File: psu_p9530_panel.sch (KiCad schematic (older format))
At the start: 58 parts, among them IC306 LTC1658, IC308 CD4052B, IC310 TLC272, IC312 TLC272, U401 54LS164

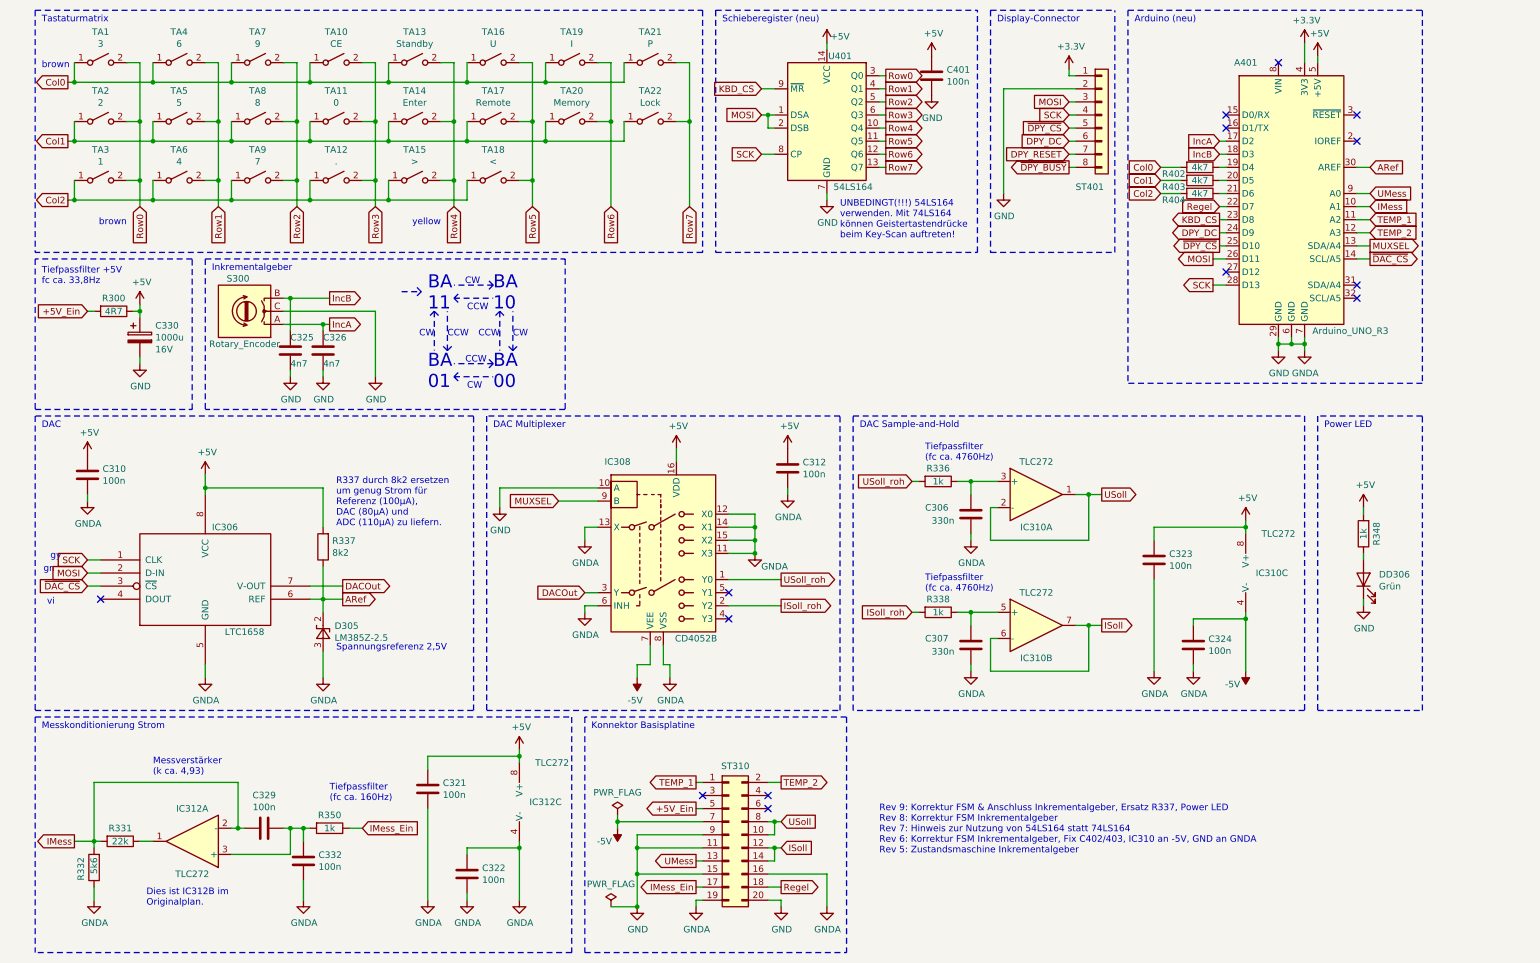
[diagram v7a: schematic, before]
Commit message: Schematic update: Display Shield Connections
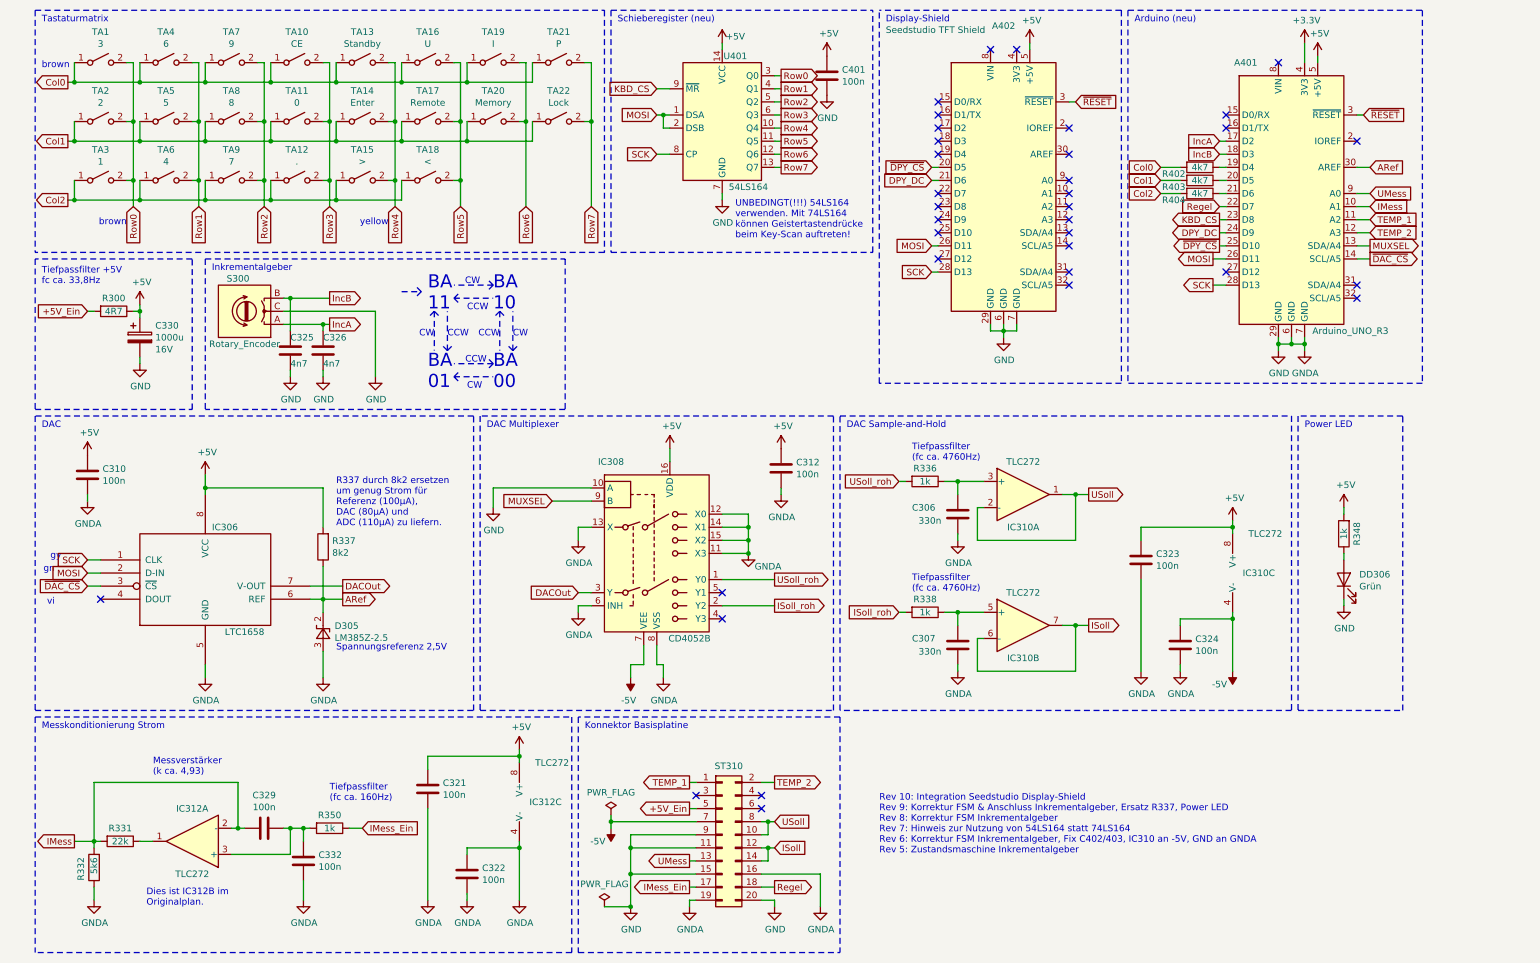
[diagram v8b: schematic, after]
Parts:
- removed ST401: Conn_01x08, symbol Connector_Generic:Conn_01x08
- added A402: Seedstudio TFT Shield, Module:Arduino_UNO_R3, symbol MCU_Module:Arduino_UNO_R3
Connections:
- net +5V: now also A402.5 (+5V)
- net DPY_DC: now also A402.21 (D6)
- net GND: now also A402.29 (GND), A402.6 (GND), A402.7 (GND)
- net MOSI: now also A402.26 (D11)
- net SCK: now also A402.28 (D13)
- net ~DPY_CS: now also A402.20 (D5)
- net ~RESET: now reaches A401.3 (~RESET)
- net ~RESET: now also A402.3 (~RESET)
- no-connect marks 14 -> 35
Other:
- note added: "Display-Shield"
- note added: "Rev 10: Integration Seedstudio Display-Shield\nRev 9: Korrektur FSM & Anschluss Inkrementalgeber, Ersatz R337, Power LED\nRev 8: Korrektur FSM Inkrementalgeber\nRev 7: Hinweis zur Nutzung von 54LS164 statt 74LS164\nRev 6: Korrektur FSM Inkrementalgeber, Fix C402/403, IC310 an -5V, GND an GNDA\nRev 5: Zustandsmaschine Inkrementalgeber"
- note removed: "Display-Connector"
- note removed: "Rev 9: Korrektur FSM & Anschluss Inkrementalgeber, Ersatz R337, Power LED\nRev 8: Korrektur FSM Inkrementalgeber\nRev 7: Hinweis zur Nutzung von 54LS164 statt 74LS164\nRev 6: Korrektur FSM Inkrementalgeber, Fix C402/403, IC310 an -5V, GND an GNDA\nRev 5: Zustandsmaschine Inkrementalgeber"
- moved on the sheet: C306, C307, C312, C323, C324, C401, DD306, IC308, IC310A, IC310B, IC310C, R336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
